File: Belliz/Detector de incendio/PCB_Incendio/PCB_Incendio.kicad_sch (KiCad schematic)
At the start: 25 parts, among them J3 KRE_3_vias, J4 KRE_3_vias, J5 KRE_3_vias, J7 KRE_3_vias, K2 AX1RC2, Q1 BC817, Q2 BC817, U1 CNY17-1, U2 CNY17-1

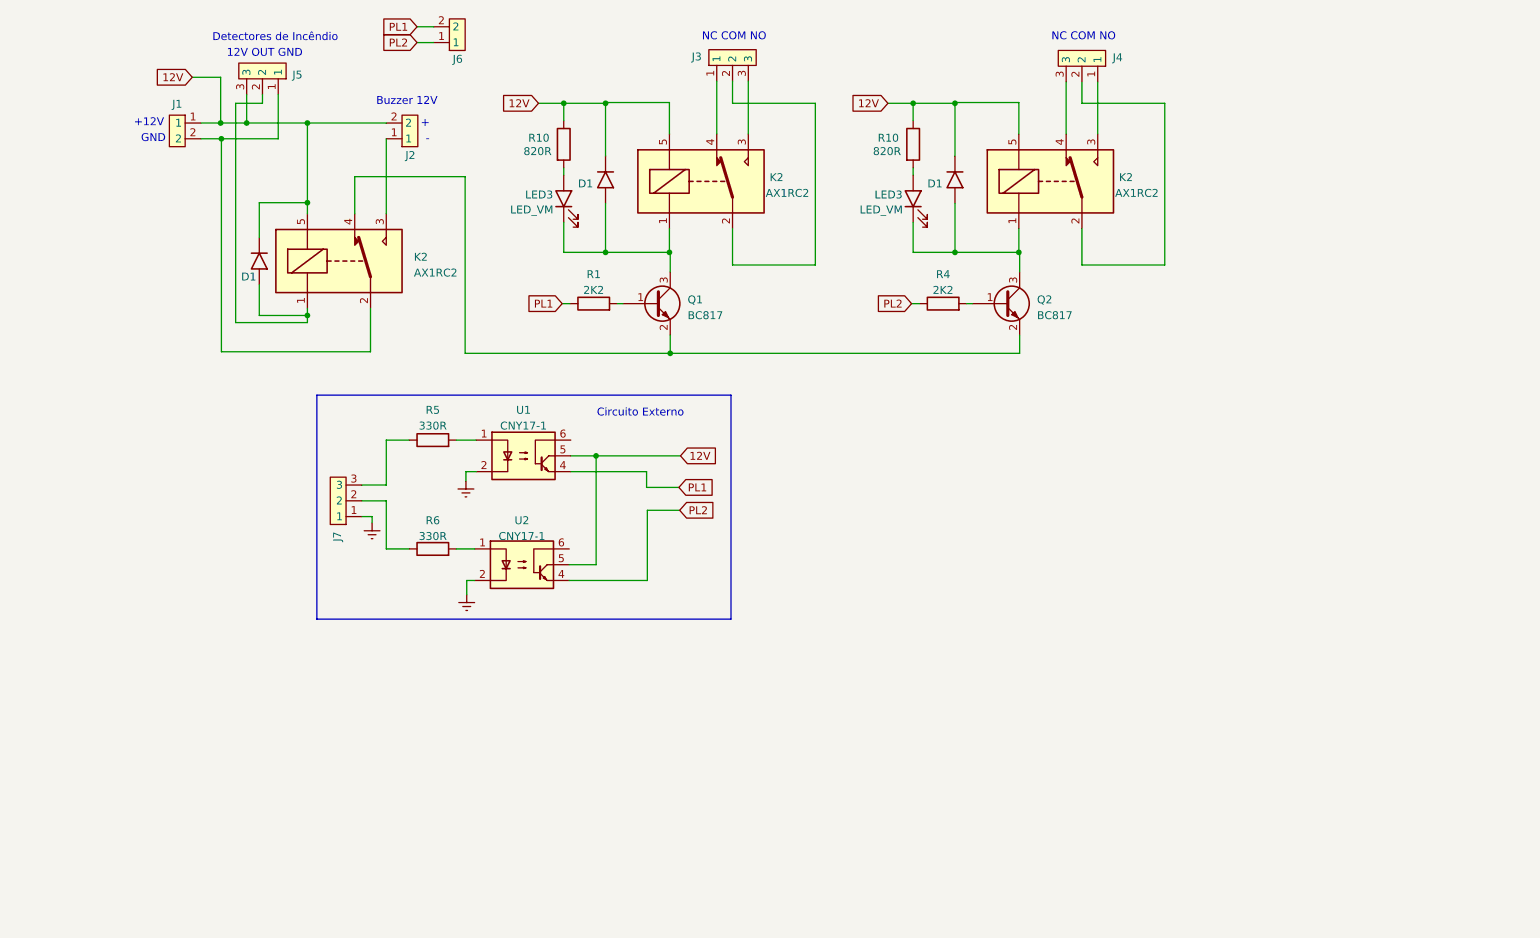
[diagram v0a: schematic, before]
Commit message: Sensor de incêncio e leds
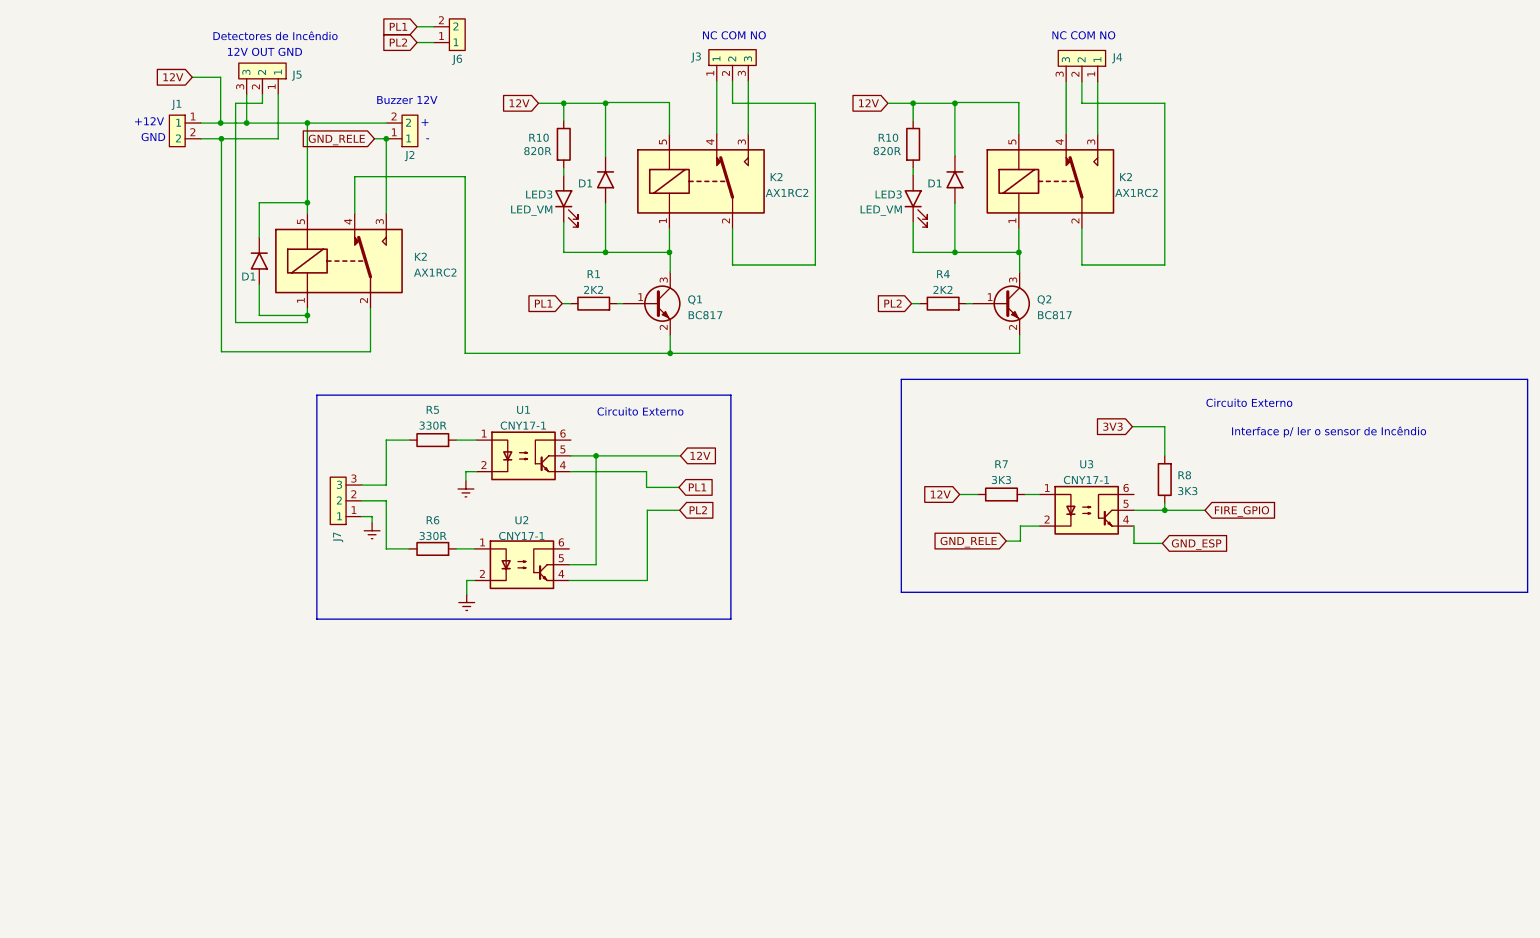
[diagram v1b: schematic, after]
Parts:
- added R7, R8: 3K3, symbol Device:R
- added U3: CNY17-1, symbol Isolator:CNY17-1
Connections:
- net 12V: now also R7.1
- net GND_RELE: now reaches J2.1, K2.3
- net GND_RELE: now also U3.2
- new net: R7.2, U3.1
- new net 3V3: R8.2
- new net FIRE_GPIO: R8.1, U3.5
- new net GND_ESP: U3.4
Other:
- note added: "Interface p/ ler o sensor de Incêndio"
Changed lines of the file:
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@@
   (junction (at 52.07 52.832) (diameter 0) (color 0 0 0 0)
   )
+  (junction (at 203.962 112.649) (diameter 0) (color 0 0 0 0)
+  )
   (junction (at 170.18 47.117) (diameter 0) (color 0 0 0 0)
   )
@@
   (junction (at 113.919 71.12) (diameter 0) (color 0 0 0 0)
   )
+  (junction (at 78.613 52.832) (diameter 0) (color 0 0 0 0)
+  )
   (junction (at 112.395 103.886) (diameter 0) (color 0 0 0 0)
   )
@@
     (stroke (width 0) (type default))
   )
+  (wire (pts (xy 180.721 115.189) (xy 183.769 115.189))
+    (stroke (width 0) (type default))
+  )
   (wire (pts (xy 188.087 52.07) (xy 188.087 43.688))
     (stroke (width 0) (type default))
   )
+  (wire (pts (xy 203.962 112.649) (xy 199.009 112.649))
+    (stroke (width 0) (type default))
+  )
   (wire (pts (xy 47.371 42.926) (xy 51.943 42.926))
     (stroke (width 0) (type default))
   )
+  (wire (pts (xy 198.755 99.187) (xy 203.962 99.187))
+    (stroke (width 0) (type default))
+  )
   (wire (pts (xy 83.566 37.338) (xy 86.233 37.338))
     (stroke (width 0) (type default))
@@
     (stroke (width 0) (type default))
   )
+  (wire (pts (xy 199.009 115.189) (xy 199.009 117.983))
+    (stroke (width 0) (type default))
+  )
   (wire (pts (xy 112.395 121.412) (xy 112.395 103.886))
     (stroke (width 0) (type default))
@@
     (stroke (width 0) (type default))
   )
+  (wire (pts (xy 199.009 117.983) (xy 203.581 117.983))
+    (stroke (width 0) (type default))
+  )
   (wire (pts (xy 113.919 47.117) (xy 113.919 55.626))
     (stroke (width 0) (type default))
@@
     (stroke (width 0) (type default))
   )
+  (wire (pts (xy 203.962 111.506) (xy 203.962 112.649))
+    (stroke (width 0) (type default))
+  )
   (wire (pts (xy 91.44 107.95) (xy 91.44 106.426))
     (stroke (width 0) (type default))
@@
     (stroke (width 0) (type default))
   )
+  (wire (pts (xy 178.435 117.602) (xy 180.721 117.602))
+    (stroke (width 0) (type default))
+  )
   (wire (pts (xy 92.837 123.952) (xy 91.567 123.952))
     (stroke (width 0) (type default))
@@
     (stroke (width 0) (type default))
   )
+  (wire (pts (xy 203.962 112.649) (xy 210.439 112.649))
+    (stroke (width 0) (type default))
+  )
   (wire (pts (xy 89.916 118.872) (xy 92.837 118.872))
     (stroke (width 0) (type default))
@@
     (stroke (width 0) (type default))
   )
+  (wire (pts (xy 203.962 99.187) (xy 203.962 103.886))
+    (stroke (width 0) (type default))
+  )
   (wire (pts (xy 58.166 76.327) (xy 58.166 81.28))
     (stroke (width 0) (type default))
@@
     (stroke (width 0) (type default))
   )
+  (wire (pts (xy 76.708 52.832) (xy 78.613 52.832))
+    (stroke (width 0) (type default))
+  )
   (wire (pts (xy 82.296 101.346) (xy 78.613 101.346))
     (stroke (width 0) (type default))
@@
     (stroke (width 0) (type default))
   )
+  (wire (pts (xy 78.613 52.832) (xy 78.74 52.832))
+    (stroke (width 0) (type default))
+  )
   (wire (pts (xy 180.594 71.12) (xy 180.467 71.12))
     (stroke (width 0) (type default))
@@
     (stroke (width 0) (type default))
   )
+  (wire (pts (xy 170.942 110.109) (xy 173.863 110.109))
+    (stroke (width 0) (type default))
+  )
   (wire (pts (xy 134.366 67.31) (xy 134.366 73.152))
     (stroke (width 0) (type default))
   )
+  (wire (pts (xy 180.721 117.602) (xy 180.721 115.189))
+    (stroke (width 0) (type default))
+  )
   (wire (pts (xy 52.07 52.832) (xy 61.214 52.832))
     (stroke (width 0) (type default))
@@
     (stroke (width 0) (type default))
   )
+  (wire (pts (xy 181.483 110.109) (xy 183.769 110.109))
+    (stroke (width 0) (type default))
+  )
   (wire (pts (xy 107.188 57.531) (xy 107.188 58.674))
     (stroke (width 0) (type default))
@@
   (wire (pts (xy 170.18 63.246) (xy 170.18 71.12))
     (stroke (width 0) (type default))
+  )
+  (rectangle (start 161.544 91.567) (end 262.382 125.857)
+    (stroke (width 0) (type default))
+    (fill (type none))
   )
   (rectangle (start 67.437 94.107) (end 134.112 130.175)
@@
     (effects (font (size 1.27 1.27)) (justify left bottom))
   )
+  (text "Circuito Externo" (at 210.566 96.393 0)
+    (effects (font (size 1.27 1.27)) (justify left bottom))
+  )
   (text "NC COM NO" (at 139.827 37.211 0)
     (effects (font (size 1.27 1.27)) (justify right bottom))
@@
   (text "NC COM NO" (at 196.088 37.211 0)
     (effects (font (size 1.27 1.27)) (justify right bottom))
+  )
+  (text "Interface p/ ler o sensor de Incêndio" (at 214.63 100.965 0)
+    (effects (font (size 1.27 1.27)) (justify left bottom))
+  )
+  (global_label "GND_RELE" (shape input) (at 178.435 117.602 180) (fields_autoplaced)
+    (effects (font (size 1.27 1.27)) (justify right))
+    (property "Intersheetrefs" "${INTERSHEET_REFS}" (at 166.095 117.602 0)
+      (effects (font (size 1.27 1.27)) (justify right) hide)
+    )
   )
   (global_label "PL1" (shape input) (at 83.566 34.798 180) (fields_autoplaced)
@@
     )
   )
+  (global_label "12V" (shape input) (at 170.942 110.109 180) (fields_autoplaced)
+    (effects (font (size 1.27 1.27)) (justify right))
+    (property "Intersheetrefs" "${INTERSHEET_REFS}" (at 164.5286 110.109 0)
+      (effects (font (size 1.27 1.27)) (justify right) hide)
+    )
+  )
+  (global_label "FIRE_GPIO" (shape input) (at 210.439 112.649 0) (fields_autoplaced)
+    (effects (font (size 1.27 1.27)) (justify left))
+    (property "Intersheetrefs" "${INTERSHEET_REFS}" (at 222.9001 112.649 0)
+      (effects (font (size 1.27 1.27)) (justify left) hide)
+    )
+  )
+  (global_label "3V3" (shape input) (at 198.755 99.187 180) (fields_autoplaced)
+    (effects (font (size 1.27 1.27)) (justify right))
+    (property "Intersheetrefs" "${INTERSHEET_REFS}" (at 192.3416 99.187 0)
+      (effects (font (size 1.27 1.27)) (justify right) hide)
+    )
+  )
   (global_label "PL1" (shape input) (at 125.73 108.966 0) (fields_autoplaced)
     (effects (font (size 1.27 1.27)) (justify left))
@@
     (property "Intersheetrefs" "${INTERSHEET_REFS}" (at 152.9716 47.117 0)
       (effects (font (size 1.27 1.27)) (justify right) hide)
+    )
+  )
+  (global_label "GND_RELE" (shape input) (at 76.708 52.832 180) (fields_autoplaced)
+    (effects (font (size 1.27 1.27)) (justify right))
+    (property "Intersheetrefs" "${INTERSHEET_REFS}" (at 64.368 52.832 0)
+      (effects (font (size 1.27 1.27)) (justify right) hide)
+    )
+  )
+  (global_label "GND_ESP" (shape input) (at 203.581 117.983 0) (fields_autoplaced)
+    (effects (font (size 1.27 1.27)) (justify left))
+    (property "Intersheetrefs" "${INTERSHEET_REFS}" (at 214.9534 117.983 0)
+      (effects (font (size 1.27 1.27)) (justify left) hide)
     )
   )
@@
     )
   )
+  (symbol (lib_id "Device:R") (at 203.962 107.696 180) (unit 1)
+    (in_bom yes) (on_board yes) (dnp no) (fields_autoplaced)
+    (property "Reference" "R8" (at 205.994 107.061 0)
+      (effects (font (size 1.27 1.27)) (justify right))
+    )
+    (property "Value" "3K3" (at 205.994 109.601 0)
+      (effects (font (size 1.27 1.27)) (justify right))
+    )
+    (property "Footprint" "" (at 205.74 107.696 90)
+      (effects (font (size 1.27 1.27)) hide)
+    )
+    (property "Datasheet" "~" (at 203.962 107.696 0)
+      (effects (font (size 1.27 1.27)) hide)
+    )
+    (pin "1")
+    (pin "2")
+    (instances
+      (project "PCB_Incendio"
+        (path "/cf7c55a1-a06f-489d-9122-7ed02b58798e"
+          (reference "R8") (unit 1)
+        )
+      )
+    )
+  )
   (symbol (lib_id "My_Library_Conectors:KRE_3_vias") (at 70.866 112.395 270) (mirror x) (unit 1)
     (in_bom yes) (on_board yes) (dnp no)
@@
         )
       )
+    )
+  )
+  (symbol (lib_id "Isolator:CNY17-1") (at 191.389 112.649 0) (unit 1)
+    (in_bom yes) (on_board yes) (dnp no) (fields_autoplaced)
+    (property "Reference" "U3" (at 191.389 105.283 0)
+      (effects (font (size 1.27 1.27)))
+    )
+    (property "Value" "CNY17-1" (at 191.389 107.823 0)
+      (effects (font (size 1.27 1.27)))
+    )
+    (property "Footprint" "" (at 191.389 112.649 0)
+      (effects (font (size 1.27 1.27)) (justify left) hide)
+    )
+    (property "Datasheet" "http://www.vishay.com/docs/83606/cny17.pdf" (at 191.389 112.649 0)
+      (effects (font (size 1.27 1.27)) (justify left) hide)
+    )
+    (pin "1")
+    (pin "2")
+    (pin "3")
+    (pin "4")
+    (pin "5")
+    (pin "6")
+    (instances
+      (project "PCB_Incendio"
+        (path "/cf7c55a1-a06f-489d-9122-7ed02b58798e"
+          (reference "U3") (unit 1)
+        )
+      )
+    )
+  )
+  (symbol (lib_id "Device:R") (at 177.673 110.109 90) (unit 1)
+    (in_bom yes) (on_board yes) (dnp no) (fields_autoplaced)
+    (property "Reference" "R7" (at 177.673 105.283 90)
+      (effects (font (size 1.27 1.27)))
+    )
+    (property "Value" "3K3" (at 177.673 107.823 90)
+      (effects (font (size 1.27 1.27)))
+    )
+    (property "Footprint" "" (at 177.673 111.887 90)
+      (effects (font (size 1.27 1.27)) hide)
+    )
+    (property "Datasheet" "~" (at 177.673 110.109 0)
+      (effects (font (size 1.27 1.27)) hide)
+    )
+    (pin "1")
+    (pin "2")
+    (instances
+      (project "PCB_Incendio"
+        (path "/cf7c55a1-a06f-489d-9122-7ed02b58798e"
+          (reference "R7") (unit 1)
+        )
+      )

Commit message: Atualização detector de incêndio
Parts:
- removed J7: KRE_3_vias, My_library_footprint:KRE_3Vias, symbol My_Library_Conectors:KRE_3_vias
- removed R5, R6: 330R, symbol Device:R
- removed U1, U2: CNY17-1, symbol Isolator:CNY17-1
- added J8: KRE_3_vias, My_library_footprint:KRE_3Vias, symbol My_Library_Conectors:KRE_3_vias
- added R10, R9: 330R, symbol Device:R
- added R11, R12, R16: 10K, symbol Device:R
- added R13: 220K, symbol Device:R
- added R14: 220R, symbol Device:R
- added U4, U5: CNY17-1, symbol Isolator:CNY17-1
- added U6: TCRT5000, symbol Isolator:CNY17-1
- R8: value 3K3 -> 10K
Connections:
- net 12V: now also R11.2, R12.2
- net 3V3: now also R14.2, R16.2
- net Earth: now also J8.1, R13.2, U4.2, U4.4, U5.2, U5.4
- net GND_RELE: now also R13.1
- net PL1: now also R11.1, U5.5
- net PL2: now also R12.1, U4.5
- new net: J8.2, R10.1
- new net: J8.3, R9.1
- new net: R10.2, U4.1
- new net: R14.1, U6.1
- new net: R9.2, U5.1
- new net GND_EXT: U6.2, U6.4
- new net OUT: R16.1, U6.5
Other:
- note added: "-3,4V"
- note added: "Circuito externo"
- note added: "Contador TCRT5000"
- note added: "Fornecer um GND para não ficar flutuando! O led poder ser acionado com corrente mínima!"
- note added: "GND 12V"
- note added: "Tinha que ser 0V ou 12V"
- moved on the sheet: R7, R8, U3
